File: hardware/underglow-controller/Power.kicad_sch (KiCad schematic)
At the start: 15 parts, among them U301 BD33C0AWFP-CE2

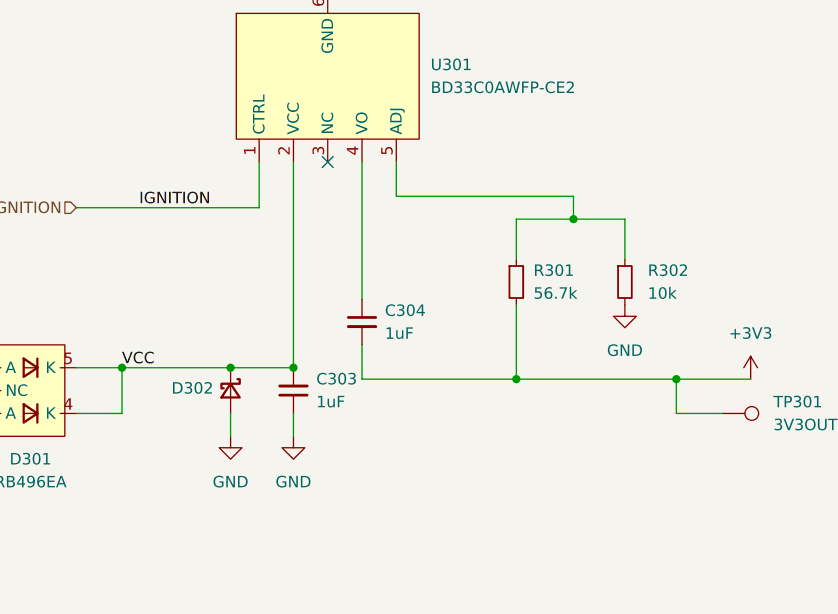
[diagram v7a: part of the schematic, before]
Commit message: hardware updates from board bringup
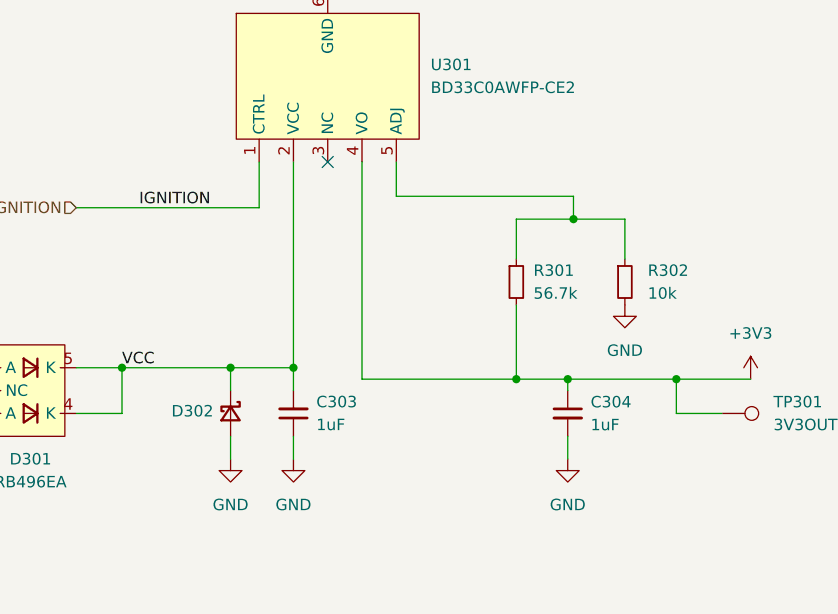
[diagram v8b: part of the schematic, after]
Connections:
- net +3V3: now also C304.1, U301.4 (VO); no longer C304.2
- net GND: now also C304.2
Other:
- moved on the sheet: C303, C304, D302
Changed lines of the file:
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@@
   (junction (at 100.965 62.23) (diameter 0) (color 0 0 0 0)
+  )
+  (junction (at 100.33 80.01) (diameter 0) (color 0 0 0 0)
   )
   (no_connect (at 73.66 55.88))
@@
     (stroke (width 0) (type default) (color 0 0 0 0))
   )
-  (wire (pts (xy 77.47 80.01) (xy 77.47 76.2))
-    (stroke (width 0) (type default) (color 0 0 0 0))
-  )
   (wire (pts (xy 27.94 78.74) (xy 33.02 78.74))
     (stroke (width 0) (type default) (color 0 0 0 0))
   )
+  (wire (pts (xy 62.865 81.28) (xy 62.865 78.74))
+    (stroke (width 0) (type default) (color 0 0 0 0))
+  )
   (wire (pts (xy 117.475 83.82) (xy 112.395 83.82))
     (stroke (width 0) (type default) (color 0 0 0 0))
@@
     (stroke (width 0) (type default) (color 0 0 0 0))
   )
-  (wire (pts (xy 77.47 55.88) (xy 77.47 71.12))
+  (wire (pts (xy 77.47 55.88) (xy 77.47 80.01))
     (stroke (width 0) (type default) (color 0 0 0 0))
   )
@@
     (stroke (width 0) (type default) (color 0 0 0 0))
   )
+  (wire (pts (xy 100.33 88.9) (xy 100.33 86.36))
+    (stroke (width 0) (type default) (color 0 0 0 0))
+  )
   (wire (pts (xy 100.965 62.23) (xy 100.965 59.69))
     (stroke (width 0) (type default) (color 0 0 0 0))
@@
     (stroke (width 0) (type default) (color 0 0 0 0))
   )
+  (wire (pts (xy 100.33 81.28) (xy 100.33 80.01))
+    (stroke (width 0) (type default) (color 0 0 0 0))
+  )
   (polyline (pts (xy 140.97 58.42) (xy 198.12 58.42))
     (stroke (width 0) (type default) (color 0 0 0 0))
@@
     (stroke (width 0) (type default) (color 0 0 0 0))
   )
-  (wire (pts (xy 62.865 83.82) (xy 62.865 86.36))
+  (wire (pts (xy 62.865 86.36) (xy 62.865 88.9))
     (stroke (width 0) (type default) (color 0 0 0 0))
   )
@@
     (stroke (width 0) (type default) (color 0 0 0 0))
   )
+  (wire (pts (xy 69.85 81.28) (xy 69.85 78.74))
+    (stroke (width 0) (type default) (color 0 0 0 0))
+  )
   (wire (pts (xy 112.395 80.01) (xy 120.65 80.01))
     (stroke (width 0) (type default) (color 0 0 0 0))
   )
-  (wire (pts (xy 69.85 86.36) (xy 69.85 83.82))
-    (stroke (width 0) (type default) (color 0 0 0 0))
-  )
-  (wire (pts (xy 94.615 80.01) (xy 112.395 80.01))
+  (wire (pts (xy 69.85 88.9) (xy 69.85 86.36))
+    (stroke (width 0) (type default) (color 0 0 0 0))
+  )
+  (wire (pts (xy 94.615 80.01) (xy 100.33 80.01))
     (stroke (width 0) (type default) (color 0 0 0 0))
   )
   (wire (pts (xy 33.02 78.74) (xy 35.56 78.74))
+    (stroke (width 0) (type default) (color 0 0 0 0))
+  )
+  (wire (pts (xy 100.33 80.01) (xy 112.395 80.01))
     (stroke (width 0) (type default) (color 0 0 0 0))
   )
@@
     (pin "2")
   )
-  (symbol (lib_id "Device:C_Small") (at 69.85 81.28 180) (unit 1)
-    (in_bom yes) (on_board yes) (fields_autoplaced)
-    (property "Reference" "C303" (id 0) (at 72.39 80.0035 0)
-      (effects (font (size 1.27 1.27)) (justify right))
-    )
-    (property "Value" "1uF" (id 1) (at 72.39 82.5435 0)
-      (effects (font (size 1.27 1.27)) (justify right))
-    )
-    (property "Footprint" "Capacitor_SMD:C_0805_2012Metric" (id 2) (at 69.85 81.28 0)
-      (effects (font (size 1.27 1.27)) hide)
-    )
-    (property "Datasheet" "~" (id 3) (at 69.85 81.28 0)
-      (effects (font (size 1.27 1.27)) hide)
-    )
-    (property "MPN" "" (id 5) (at 69.85 81.28 0)
-      (effects (font (size 1.27 1.27)) hide)
-    )
-    (property "Description" "" (id 7) (at 69.85 81.28 0)
-      (effects (font (size 1.27 1.27)) hide)
-    )
-    (pin "1")
-    (pin "2")
-  )
-  (symbol (lib_id "power:GND") (at 62.865 86.36 0) (unit 1)
-    (in_bom yes) (on_board yes) (fields_autoplaced)
-    (property "Reference" "#PWR063" (id 0) (at 62.865 92.71 0)
-      (effects (font (size 1.27 1.27)) hide)
-    )
-    (property "Value" "GND" (id 1) (at 62.865 91.44 0))
-    (property "Footprint" "" (id 2) (at 62.865 86.36 0)
-      (effects (font (size 1.27 1.27)) hide)
-    )
-    (property "Datasheet" "" (id 3) (at 62.865 86.36 0)
+  (symbol (lib_id "Device:C_Small") (at 69.85 83.82 180) (unit 1)
+    (in_bom yes) (on_board yes) (fields_autoplaced)
+    (property "Reference" "C303" (id 0) (at 72.39 82.5435 0)
+      (effects (font (size 1.27 1.27)) (justify right))
+    )
+    (property "Value" "1uF" (id 1) (at 72.39 85.0835 0)
+      (effects (font (size 1.27 1.27)) (justify right))
+    )
+    (property "Footprint" "Capacitor_SMD:C_0805_2012Metric" (id 2) (at 69.85 83.82 0)
+      (effects (font (size 1.27 1.27)) hide)
+    )
+    (property "Datasheet" "~" (id 3) (at 69.85 83.82 0)
+      (effects (font (size 1.27 1.27)) hide)
+    )
+    (property "MPN" "" (id 5) (at 69.85 83.82 0)
+      (effects (font (size 1.27 1.27)) hide)
+    )
+    (property "Description" "" (id 7) (at 69.85 83.82 0)
+      (effects (font (size 1.27 1.27)) hide)
+    )
+    (pin "1")
+    (pin "2")
+  )
+  (symbol (lib_id "power:GND") (at 62.865 88.9 0) (unit 1)
+    (in_bom yes) (on_board yes) (fields_autoplaced)
+    (property "Reference" "#PWR063" (id 0) (at 62.865 95.25 0)
+      (effects (font (size 1.27 1.27)) hide)
+    )
+    (property "Value" "GND" (id 1) (at 62.865 93.98 0))
+    (property "Footprint" "" (id 2) (at 62.865 88.9 0)
+      (effects (font (size 1.27 1.27)) hide)
+    )
+    (property "Datasheet" "" (id 3) (at 62.865 88.9 0)
+      (effects (font (size 1.27 1.27)) hide)
+    )
+    (pin "1")
+  )
+  (symbol (lib_id "power:GND") (at 100.33 88.9 0) (unit 1)
+    (in_bom yes) (on_board yes) (fields_autoplaced)
+    (property "Reference" "#PWR0103" (id 0) (at 100.33 95.25 0)
+      (effects (font (size 1.27 1.27)) hide)
+    )
+    (property "Value" "GND" (id 1) (at 100.33 93.98 0))
+    (property "Footprint" "" (id 2) (at 100.33 88.9 0)
+      (effects (font (size 1.27 1.27)) hide)
+    )
+    (property "Datasheet" "" (id 3) (at 100.33 88.9 0)
       (effects (font (size 1.27 1.27)) hide)
     )
@@
     (pin "5")
   )
-  (symbol (lib_id "power:GND") (at 69.85 86.36 0) (unit 1)
-    (in_bom yes) (on_board yes) (fields_autoplaced)
-    (property "Reference" "#PWR064" (id 0) (at 69.85 92.71 0)
-      (effects (font (size 1.27 1.27)) hide)
-    )
-    (property "Value" "GND" (id 1) (at 69.85 91.44 0))
-    (property "Footprint" "" (id 2) (at 69.85 86.36 0)
-      (effects (font (size 1.27 1.27)) hide)
-    )
-    (property "Datasheet" "" (id 3) (at 69.85 86.36 0)
-      (effects (font (size 1.27 1.27)) hide)
-    )
-    (pin "1")
-  )
-  (symbol (lib_id "Device:C_Small") (at 77.47 73.66 0) (unit 1)
-    (in_bom yes) (on_board yes) (fields_autoplaced)
-    (property "Reference" "C304" (id 0) (at 80.01 72.3962 0)
-      (effects (font (size 1.27 1.27)) (justify left))
-    )
-    (property "Value" "1uF" (id 1) (at 80.01 74.9362 0)
-      (effects (font (size 1.27 1.27)) (justify left))
-    )
-    (property "Footprint" "Capacitor_SMD:C_0805_2012Metric" (id 2) (at 77.47 73.66 0)
-      (effects (font (size 1.27 1.27)) hide)
-    )
-    (property "Datasheet" "~" (id 3) (at 77.47 73.66 0)
-      (effects (font (size 1.27 1.27)) hide)
-    )
-    (property "MPN" "" (id 5) (at 77.47 73.66 0)
-      (effects (font (size 1.27 1.27)) hide)
-    )
-    (property "Description" "" (id 6) (at 77.47 73.66 0)
+  (symbol (lib_id "power:GND") (at 69.85 88.9 0) (unit 1)
+    (in_bom yes) (on_board yes) (fields_autoplaced)
+    (property "Reference" "#PWR064" (id 0) (at 69.85 95.25 0)
+      (effects (font (size 1.27 1.27)) hide)
+    )
+    (property "Value" "GND" (id 1) (at 69.85 93.98 0))
+    (property "Footprint" "" (id 2) (at 69.85 88.9 0)
+      (effects (font (size 1.27 1.27)) hide)
+    )
+    (property "Datasheet" "" (id 3) (at 69.85 88.9 0)
+      (effects (font (size 1.27 1.27)) hide)
+    )
+    (pin "1")
+  )
+  (symbol (lib_id "Device:C_Small") (at 100.33 83.82 0) (unit 1)
+    (in_bom yes) (on_board yes) (fields_autoplaced)
+    (property "Reference" "C304" (id 0) (at 102.87 82.5562 0)
+      (effects (font (size 1.27 1.27)) (justify left))
+    )
+    (property "Value" "1uF" (id 1) (at 102.87 85.0962 0)
+      (effects (font (size 1.27 1.27)) (justify left))
+    )
+    (property "Footprint" "Capacitor_SMD:C_0805_2012Metric" (id 2) (at 100.33 83.82 0)
+      (effects (font (size 1.27 1.27)) hide)
+    )
+    (property "Datasheet" "~" (id 3) (at 100.33 83.82 0)
+      (effects (font (size 1.27 1.27)) hide)
+    )
+    (property "MPN" "" (id 5) (at 100.33 83.82 0)
+      (effects (font (size 1.27 1.27)) hide)
+    )
+    (property "Description" "" (id 6) (at 100.33 83.82 0)
       (effects (font (size 1.27 1.27)) hide)
     )
@@
     (pin "2")
   )
-  (symbol (lib_id "Device:D_Schottky_Small") (at 62.865 81.28 270) (unit 1)
-    (in_bom yes) (on_board yes) (fields_autoplaced)
-    (property "Reference" "D302" (id 0) (at 60.96 81.0259 90)
-      (effects (font (size 1.27 1.27)) (justify right))
-    )
-    (property "Value" "D_Schottky_Small" (id 1) (at 60.325 79.7561 90)
+  (symbol (lib_id "Device:D_Schottky_Small") (at 62.865 83.82 270) (unit 1)
+    (in_bom yes) (on_board yes) (fields_autoplaced)
+    (property "Reference" "D302" (id 0) (at 60.96 83.5659 90)
+      (effects (font (size 1.27 1.27)) (justify right))
+    )
+    (property "Value" "D_Schottky_Small" (id 1) (at 60.325 82.2961 90)
       (effects (font (size 1.27 1.27)) (justify right) hide)
     )
-    (property "Footprint" "Diode_SMD:D_SMA" (id 2) (at 62.865 81.28 90)
-      (effects (font (size 1.27 1.27)) hide)
-    )
-    (property "Datasheet" "~" (id 3) (at 62.865 81.28 90)
-      (effects (font (size 1.27 1.27)) hide)
-    )
-    (property "MPN" "BYS10-45HE3_A/H" (id 4) (at 62.865 81.28 0)
-      (effects (font (size 1.27 1.27)) hide)
-    )
+    (property "Footprint" "Diode_SMD:D_SMA" (id 2) (at 62.865 83.82 90)
+      (effects (font (size 1.27 1.27)) hide)
+    )
+    (property "Datasheet" "~" (id 3) (at 62.865 83.82 90)
+      (effects (font (size 1.27 1.27)) hide)
+    )
+    (property "MPN" "BYS10-45HE3_A/H" (id 4) (at 62.865 83.82 0)
+      (effects (font (size 1.27 1.27)) hide)
+    )
